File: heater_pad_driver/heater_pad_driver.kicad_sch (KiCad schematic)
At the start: 25 parts, among them J1 24V_IN, J2 GND_IN, J3 Heater_Conn, J4 CTL_Conn, Q1 NPN, Q2 NMOS, U1 UCC23525CDWYR, U2 ACS713xLCTR-30A

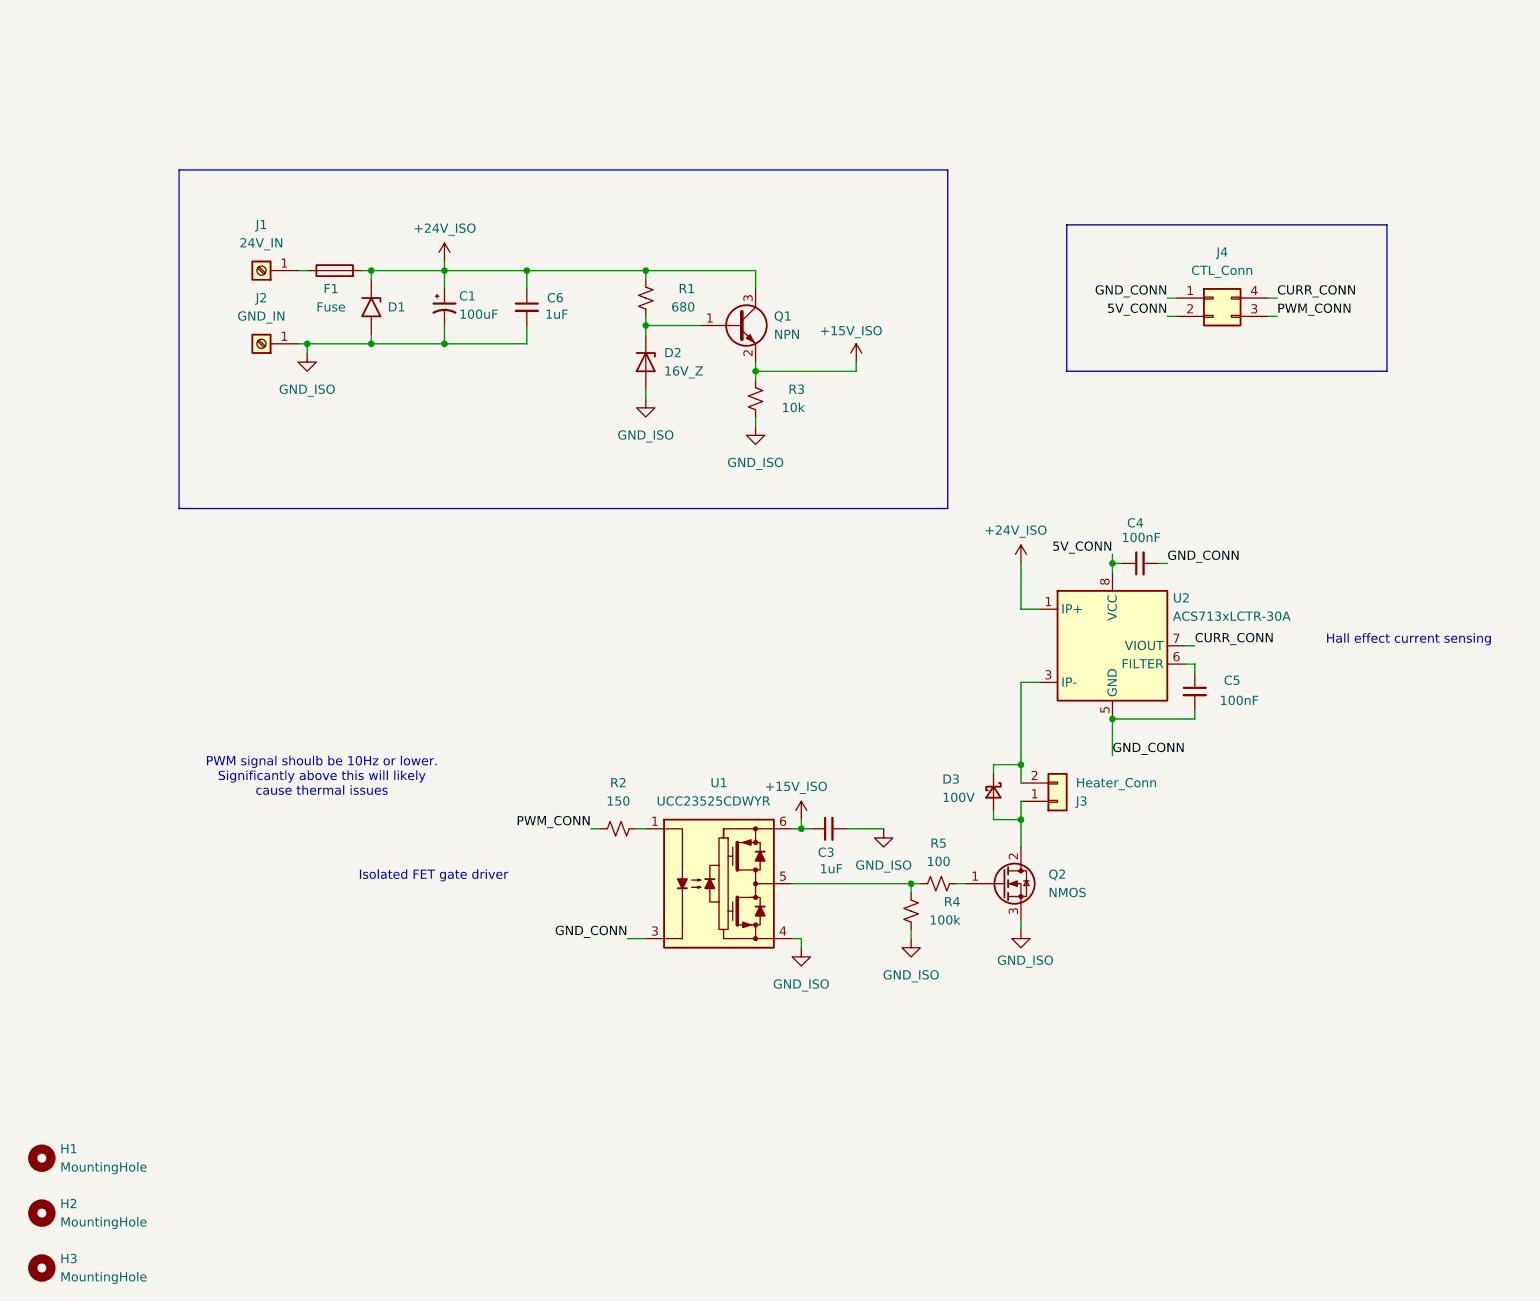
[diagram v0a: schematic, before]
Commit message: add relay to heater board for estop and do some ignitor board routing
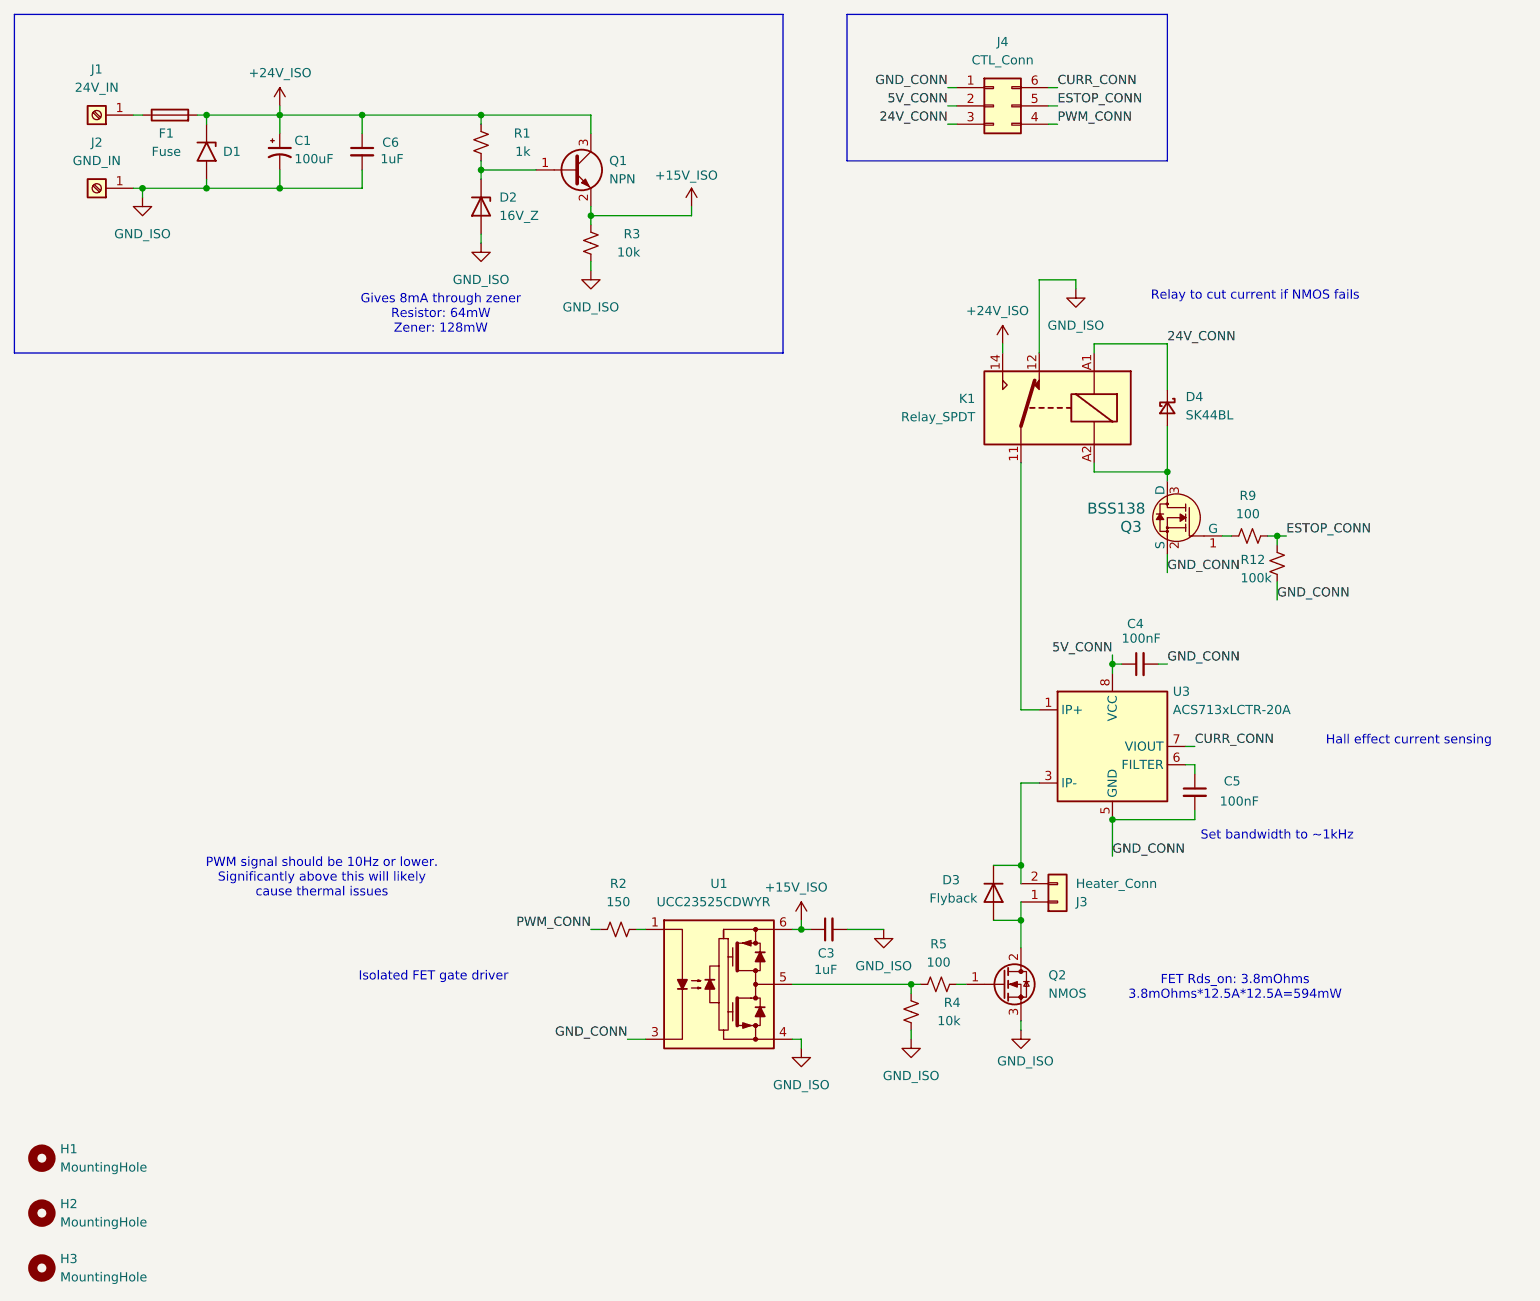
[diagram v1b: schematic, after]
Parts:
- removed U2: ACS713xLCTR-30A, Package_SO:SOIC-8_3.9x4.9mm_P1.27mm, symbol Sensor_Current:ACS713xLCTR-30A
- added D4: SK44BL, Diode_SMD:D_SMB_Handsoldering, symbol Device:D_Schottky_Small
- added K1: Relay_SPDT, Library:AZ576-1C, symbol Relay:Relay_SPDT
- added Q3: BSS138, Package_TO_SOT_SMD:SOT-23, symbol dk_Transistors-FETs-MOSFETs-Single:BSS138
- added R12: 100k, Resistor_SMD:R_0805_2012Metric_Pad1.20x1.40mm_HandSolder, symbol Device:R_Small_US
- added R9: 100, Resistor_SMD:R_0805_2012Metric_Pad1.20x1.40mm_HandSolder, symbol Device:R_Small_US
- added U3: ACS713xLCTR-20A, Package_SO:SOIC-8_3.9x4.9mm_P1.27mm, symbol Sensor_Current:ACS713xLCTR-20A
- D3: value 100V -> Flyback; footprint Diode_SMD:D_SMA_Handsoldering -> Package_TO_SOT_THT:TO-220F-2_Vertical; symbol Device:D_Schottky_Small -> Device:D; MPN SS510 -> SDURK20Q60
- J2: MPN (none) -> AMT0440007DB0000G
- J4: footprint Connector_Molex:Molex_Micro-Fit_3.0_43045-0412_2x02_P3.00mm_Vertical -> Connector_Molex:Molex_Micro-Fit_3.0_43045-0612_2x03_P3.00mm_Vertical; symbol Connector_Generic:Conn_02x02_Counter_Clockwise -> Connector_Generic:Conn_02x03_Counter_Clockwise
- Q2: MPN DMTH6005LK3-13 -> DMTH6004SK3Q-13
- R1: value 680 -> 1k
- R4: value 100k -> 10k
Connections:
- net +24V_ISO: now also K1.14
- net 5V_CONN: now also U3.8 (VCC)
- net CURR_CONN: now also J4.6 (Pin_6), U3.7 (VIOUT); no longer J4.4 (Pin_4)
- net GND_CONN: now also Q3.2 (S), R12.2, U3.5 (GND)
- net GND_ISO: now also K1.12
- net PWM_CONN: now also J4.4 (Pin_4); no longer J4.3 (Pin_3)
- net at D3.1 (K), J3.2 (Pin_2): now also U3.3 (IP-), U3.4 (IP-)
- net at C5.1: now also U3.6 (FILTER)
- new net: Q3.1 (G), R9.1
- new net: K1.11, U3.1 (IP+), U3.2 (IP+)
- new net: D4.2 (A), K1.A2, Q3.3 (D)
- new net 24V_CONN: D4.1 (K), J4.3 (Pin_3), K1.A1
- new net ESTOP_CONN: J4.5 (Pin_5), R12.1, R9.2
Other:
- note added: "FET Rds_on: 3.8mOhms 3.8mOhms*12.5A*12.5A=594mW"
- note added: "Gives 8mA through zener Resistor: 64mW Zener: 128mW"
- note added: "PWM signal should be 10Hz or lower. Significantly above this will likely cause thermal issues"
- note added: "Relay to cut current if NMOS fails"
- note added: "Set bandwidth to ~1kHz"
- note removed: "PWM signal shoulb be 10Hz or lower. Significantly above this will likely cause thermal issues"
- moved on the sheet: C1, C3, C4, C5, C6, D1, D2, D3, F1, J1, J2, J3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

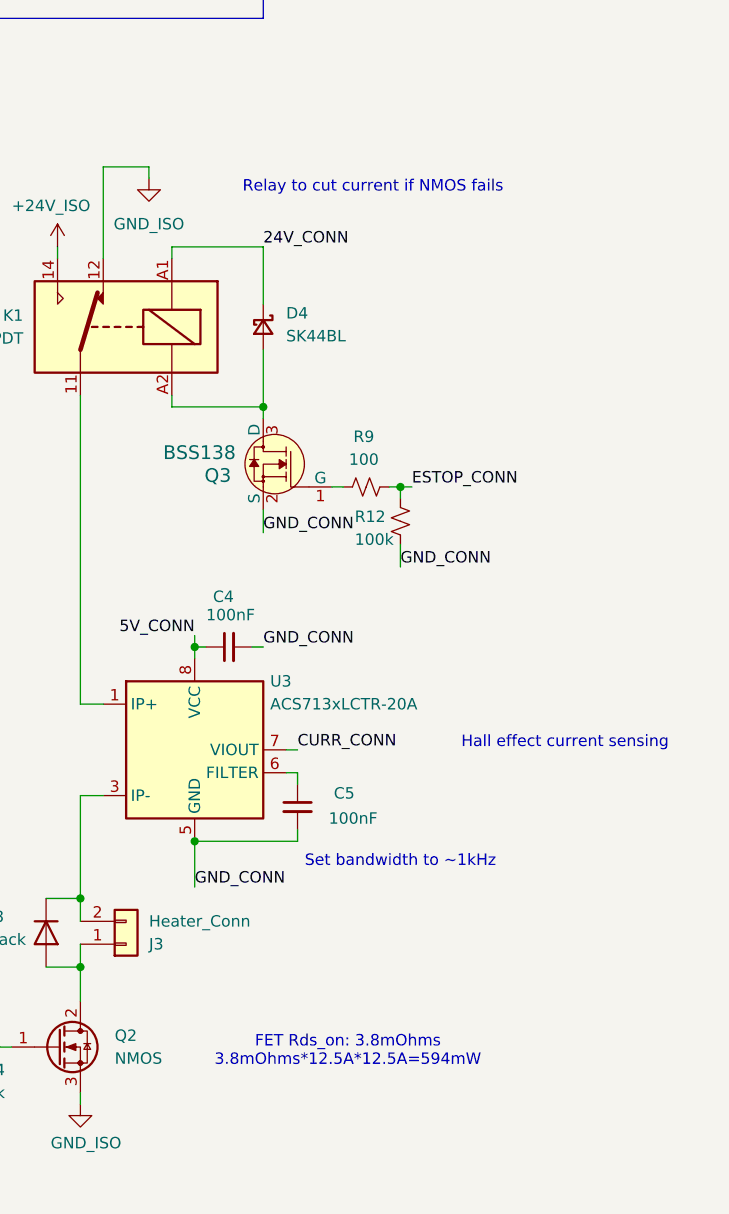
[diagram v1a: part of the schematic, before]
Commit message: finish ignitor board routing
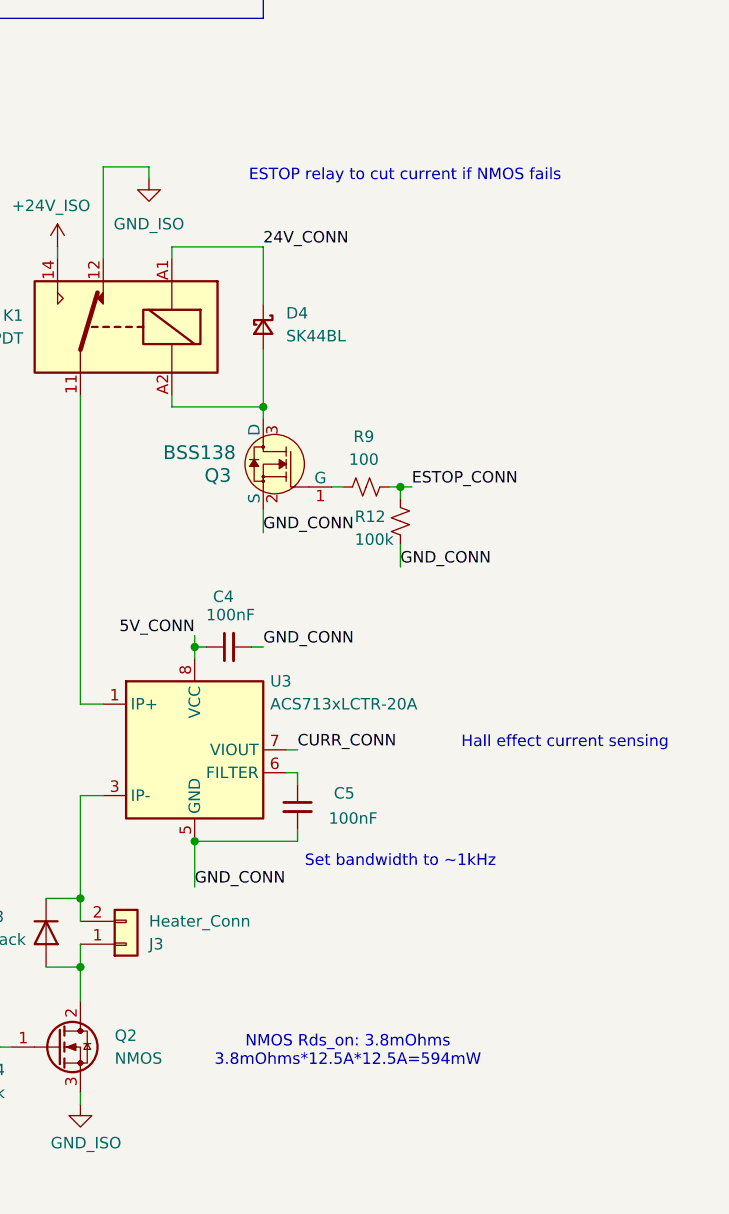
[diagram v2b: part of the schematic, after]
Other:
- note added: "ESTOP relay to cut current if NMOS fails"
- note added: "NMOS Rds_on: 3.8mOhms 3.8mOhms*12.5A*12.5A=594mW"
- note removed: "FET Rds_on: 3.8mOhms 3.8mOhms*12.5A*12.5A=594mW"
- note removed: "Relay to cut current if NMOS fails"
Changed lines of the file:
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@@
 		)
 	)
-	(text "Relay to cut current if NMOS fails"
+	(text "ESTOP relay to cut current if NMOS fails"
 		(exclude_from_sim no)
-		(at 189.992 55.626 0)
+		(at 193.548 54.356 0)
 		(effects
 			(font
@@
 		)
 	)
-	(text "FET Rds_on: 3.8mOhms\n3.8mOhms*12.5A*12.5A=594mW"
+	(text "NMOS Rds_on: 3.8mOhms\n3.8mOhms*12.5A*12.5A=594mW"
 		(exclude_from_sim no)
 		(at 187.198 151.638 0)

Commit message: updates for manufacturing
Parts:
- D1: LCSC C135156 -> (none)
- D4: value SK44BL -> SK44BL-TP
- F1: LCSC N/A -> (none)
- Q3: Description_1 MOSFET N-CH 50V 220MA SOT-23 -> (none)
- R12: LCSC C25531 -> (none); MPN 0402WGJ0103TCE -> (none)
- R9: LCSC C25076 -> (none); MPN 0402WGF1000TCE -> (none)
- U3: value ACS713xLCTR-20A -> ACS724xLCTR-30AU; symbol Sensor_Current:ACS713xLCTR-20A -> Sensor_Current:ACS724xLCTR-30AU; MPN ACS713ELCTR-20A-T -> ACS724LLCTR-30AU-T
